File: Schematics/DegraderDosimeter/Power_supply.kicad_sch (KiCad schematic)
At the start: 25 parts, among them U5 TC1262-33, U6 LM60430DRPKR, U7 TC1262-33

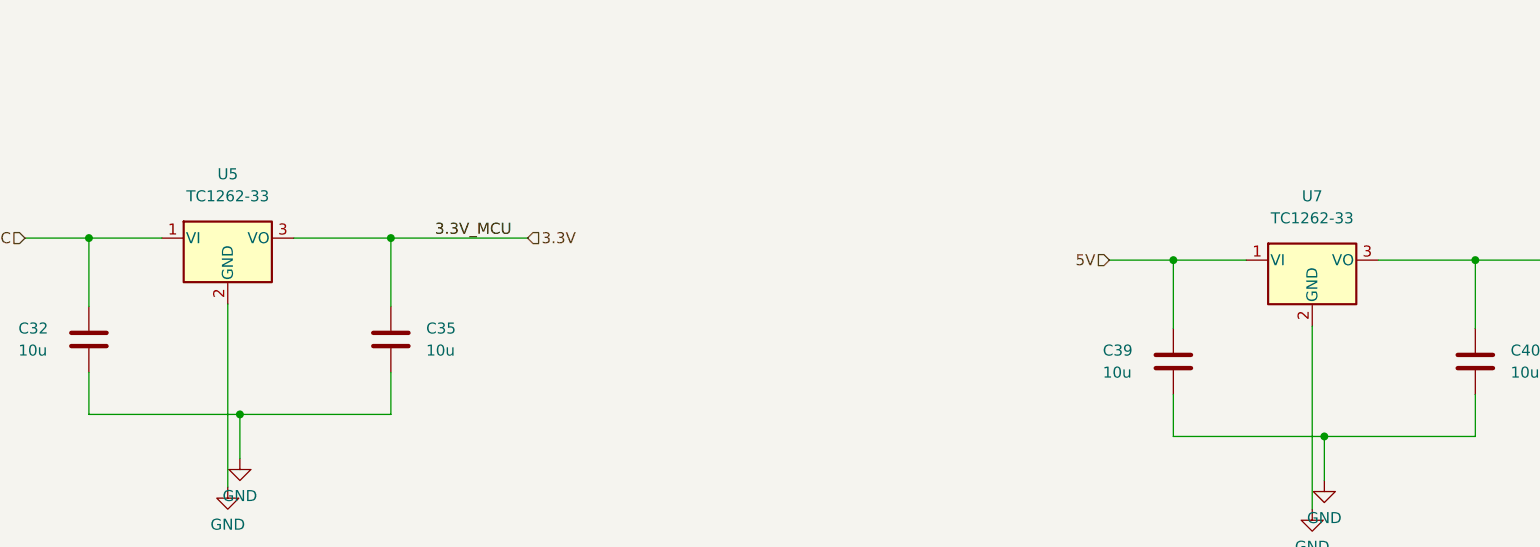
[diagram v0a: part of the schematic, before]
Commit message: Update: Combine degrader and dosimeter schematics
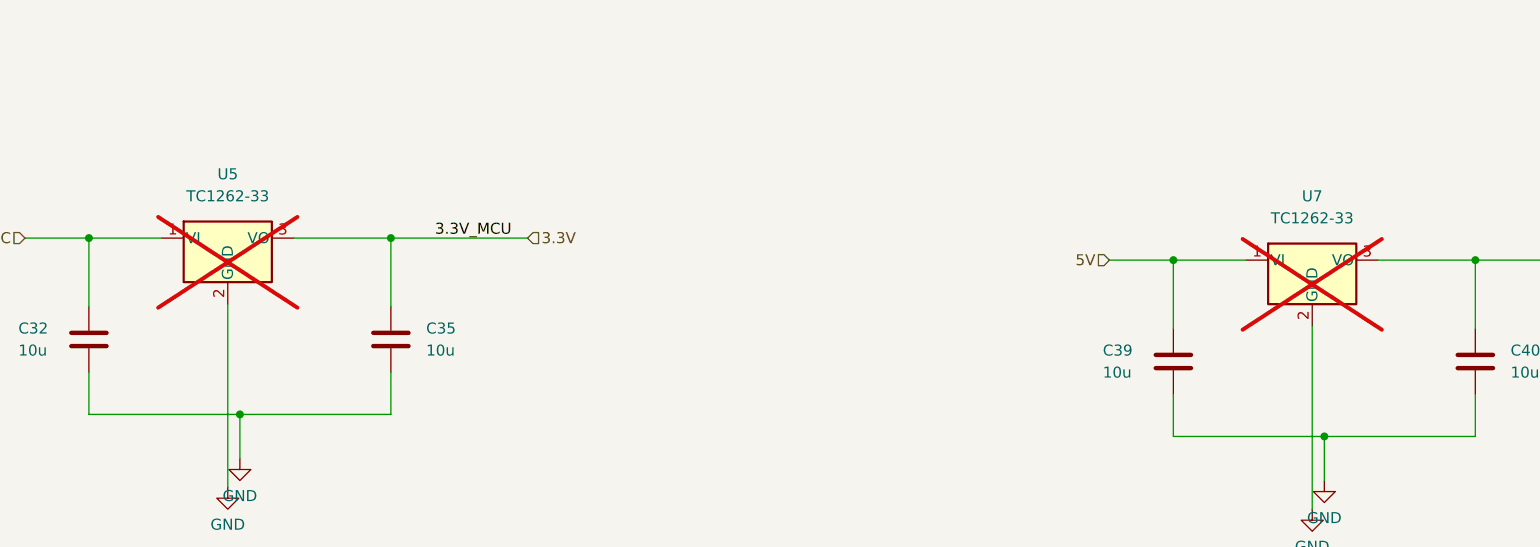
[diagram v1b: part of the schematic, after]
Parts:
- C31, C34: LCSC (none) -> C29823
- C32: footprint Capacitor_SMD:C_1206_3216Metric -> Capacitor_SMD:C_0805_2012Metric; LCSC (none) -> C440198
- C33, C35, C39, C40: footprint Capacitor_SMD:C_1206_3216Metric -> Capacitor_SMD:C_0603_1608Metric; LCSC (none) -> C19702
- C36, C37: footprint Capacitor_SMD:C_1206_3216Metric -> Capacitor_SMD:C_0805_2012Metric; LCSC (none) -> C5378
- C38: footprint Capacitor_SMD:C_1206_3216Metric -> Capacitor_SMD:C_0603_1608Metric; LCSC (none) -> C15849
- C41, C44: footprint Capacitor_SMD:C_1206_3216Metric -> Capacitor_SMD:C_0603_1608Metric; LCSC (none) -> C14663
- C42: footprint Capacitor_SMD:C_1206_3216Metric -> Capacitor_SMD:C_0603_1608Metric
- C43: LCSC (none) -> C96123
- R22: footprint Resistor_SMD:R_1206_3216Metric_Pad1.30x1.75mm_HandSolder -> Resistor_SMD:R_0603_1608Metric; LCSC (none) -> C21190
- R24, R25: footprint Resistor_SMD:R_1206_3216Metric_Pad1.30x1.75mm_HandSolder -> Resistor_SMD:R_0603_1608Metric; LCSC (none) -> C25803
- R26: footprint Resistor_SMD:R_1206_3216Metric_Pad1.30x1.75mm_HandSolder -> Resistor_SMD:R_0603_1608Metric
- U5, U7: now not fitted
